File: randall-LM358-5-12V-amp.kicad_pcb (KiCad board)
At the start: 2 copper layers, 20 parts, among them J1 IN1, J2 IN2, J3 Barrel_Jack, M1 Fan_3pin, M2 Fan_3pin, Q1 TIP120, Q2 TIP120, U3 LM358

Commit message: Footprint PCB Time
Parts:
- removed the J1 at (58.9, 5.88)
- removed J2: IN2, Connector_PinHeader_2.54mm:PinHeader_1x02_P2.54mm_Vertical
- added C1: 100uF, Capacitor_THT:CP_Radial_D5.0mm_P2.00mm, F.Cu at (92.6, 23.1)
- added C2: 0.01uF, Capacitor_THT:C_Disc_D7.5mm_W5.0mm_P5.00mm, F.Cu at (83.2, 23.1)
- added C3: 100uF, Capacitor_THT:CP_Radial_D5.0mm_P2.00mm, F.Cu at (99.2, 23.1)
- added C4: 100uF, Capacitor_THT:CP_Radial_D5.0mm_P2.00mm, F.Cu at (111.8, 19.1)
- added C5: 100uF, Capacitor_THT:CP_Radial_D5.0mm_P2.00mm, F.Cu at (118.4, 19.1)
- added D1: D_Schottky, Diode_THT:D_A-405_P7.62mm_Horizontal, F.Cu at (71.9, 22.0)
- added L1: 68uH, Inductor_THT:L_Axial_L14.0mm_D4.5mm_P5.08mm_Vertical_Fastron_LACC, F.Cu at (112.4, 12.8)
- added U1: LM2674M-3.3, Package_DIP:DIP-8_W7.62mm_Socket, F.Cu at (111.5, 0.02)
- added U3: Z-Uno, ZUno:Z-UNO, F.Cu at (89.8, 8.86)
- J1: renamed from J3; footprint Connector_BarrelJack:BarrelJack_CUI_PJ-063AH_Horizontal_CircularHoles -> TerminalBlock:TerminalBlock_Altech_AK300-2_P5.00mm
- moved Q1 118.2 mm to (128.3, 64.8)
- moved Q2 99.5 mm to (127.0, 49.5)
- moved U2 97.6 mm to (99.1, 61.0)
- moved R4 81.7 mm to (99.1, 47.0)
- moved R3 69.3 mm to (66.0, 68.6)
- moved J1 16.6 mm to (15.2, 19.1)
- renumbered D1 to D2, D2 to D3, R2 to R1, R3 to R2, R4 to R3, R1 to R4, R7 to R6, R8 to R7, R9 to R8, R6 to R9, U3 to U2
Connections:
- J1 pad 1: 10-24VDC+ -> 15VDC
- J1 pad 2: 10-24VDC- -> GND

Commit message: Ok cool
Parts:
- moved R5 217.4 mm to (212.0, 132.8), turned to 90 degrees
- moved D2 213.4 mm to (213.6, 108.8), turned to 90 degrees
- moved D3 194.8 mm to (213.5, 63.7), turned to 270 degrees
- moved M1 193.9 mm to (213.6, 114.5), turned to 270 degrees
- moved R10 191.9 mm to (212.0, 94.8), turned to 90 degrees
- moved M2 177.3 mm to (213.6, 76.5), turned to 270 degrees
- moved R6 156.6 mm to (168.3, 95.9), turned to 180 degrees
- moved R9 152.1 mm to (156.2, 105.4), turned to 180 degrees
- moved R2 148.5 mm to (155.6, 88.3), turned to 180 degrees
- moved R8 148.0 mm to (168.3, 81.3), turned to 180 degrees
- moved R1 142.2 mm to (148.0, 95.9)
- moved R7 139.1 mm to (160.7, 88.3)
- moved C4 109.0 mm to (162.6, 115.6), turned to 90 degrees
- moved U3 100.7 mm to (134.6, 99.1), turned to 270 degrees
- moved C5 97.0 mm to (162.6, 105.4), turned to 90 degrees
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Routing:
- added copper zone on B.Cu, net GND
- added copper zone on F.Cu, net GND
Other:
- board outline added: 137.2 x 91.4 mm
- net class High added: clearance 0.781437, trace_width 0.781437, via_dia 0.8, via_drill 0.4

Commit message: This is it, make no mistake about it
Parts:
- J1: value Barrel_Jack -> Power
- moved D2 39.3 mm to (175.3, 100.3), turned to 270 degrees
- moved D3 38.3 mm to (175.2, 63.1)
- moved FAN1 38.3 mm to (175.3, 113.9)
- moved FAN2 38.3 mm to (175.3, 75.8)
- moved Q1 38.3 mm to (163.4, 114.2)
- moved Q2 38.3 mm to (163.4, 77.0)
- moved R5 36.8 mm to (175.3, 132.2)
- moved R10 36.7 mm to (175.3, 94.0)
- moved C1 24.4 mm to (94.5, 81.9), turned to 0 degrees
- moved U2 20.5 mm to (137.2, 76.2)
- moved R7 19.2 mm to (144.6, 98.7)
- moved R3 19.2 mm to (131.9, 91.8)
- moved R8 19.2 mm to (152.2, 91.8)
- moved R2 19.2 mm to (139.5, 98.7)
- moved U3 18.5 mm to (116.1, 98.9)
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- renumbered M1 to FAN1, M2 to FAN2
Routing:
- net 15VDC: track 0.00 -> 223.0 mm
- net TACH2: track 0.00 -> 70.3 mm
- net TACH1: track 0.00 -> 66.4 mm
- net Net-(Q1-Pad1): track 0.00 -> 59.8 mm
- net Net-(C4-Pad1): track 0.00 -> 53.9 mm
- net Net-(C5-Pad1): track 0.00 -> 39.4 mm
- net Net-(Q2-Pad1): track 0.00 -> 35.5 mm
- net Net-(C2-Pad1): track 0.00 -> 35.3 mm
- net Net-(D2-Pad2): track 0.00 -> 32.7 mm
- net Net-(D3-Pad2): track 0.00 -> 32.1 mm
- net Net-(R2-Pad1): track 0.00 -> 21.0 mm
- net 3V3DC: track 0.00 -> 19.1 mm
- net Net-(R7-Pad1): track 0.00 -> 18.3 mm
- net PWM1: track 0.00 -> 17.5 mm
- net Net-(C2-Pad2): track 0.00 -> 16.1 mm
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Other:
- board size 137.2 x 91.4 mm -> 100.3 x 77.5 mm
- net class Default: clearance 0.2 -> 0.25; trace_width 0.25 -> 0.127; via_dia 0.8 -> 0.6; via_drill 0.4 -> 0.3
- net class High removed
- rule trace_clearance: 0.2 -> 0.25
- rule trace_min: 0.2 -> 0.127
- rule via_min_size: 0.4 -> 0.6
- board text added: "15VDC"
- board text added: "Fan Controller Board"
- board text added: "GND"
- board text added: "Randall Shutt"
- board text added: "Version 0.0.1"

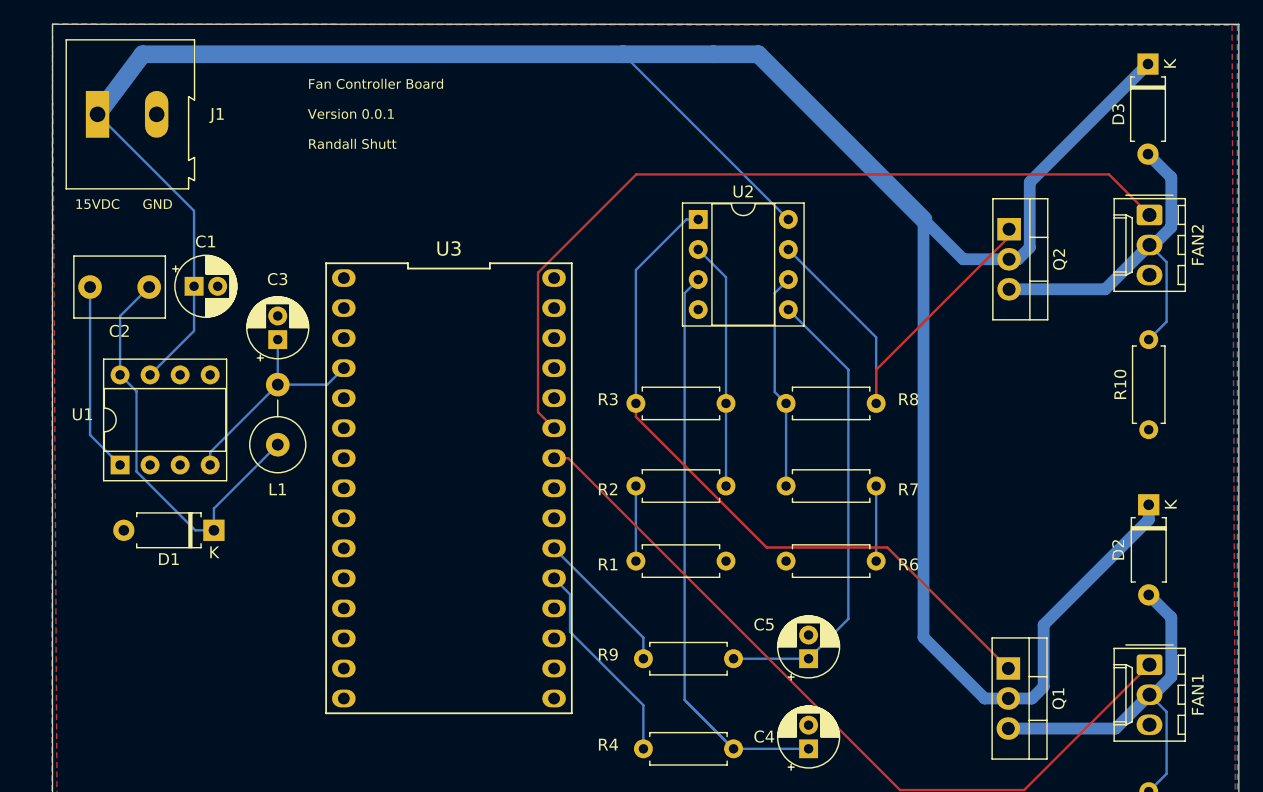
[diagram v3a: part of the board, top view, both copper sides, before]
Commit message: Added zuno module
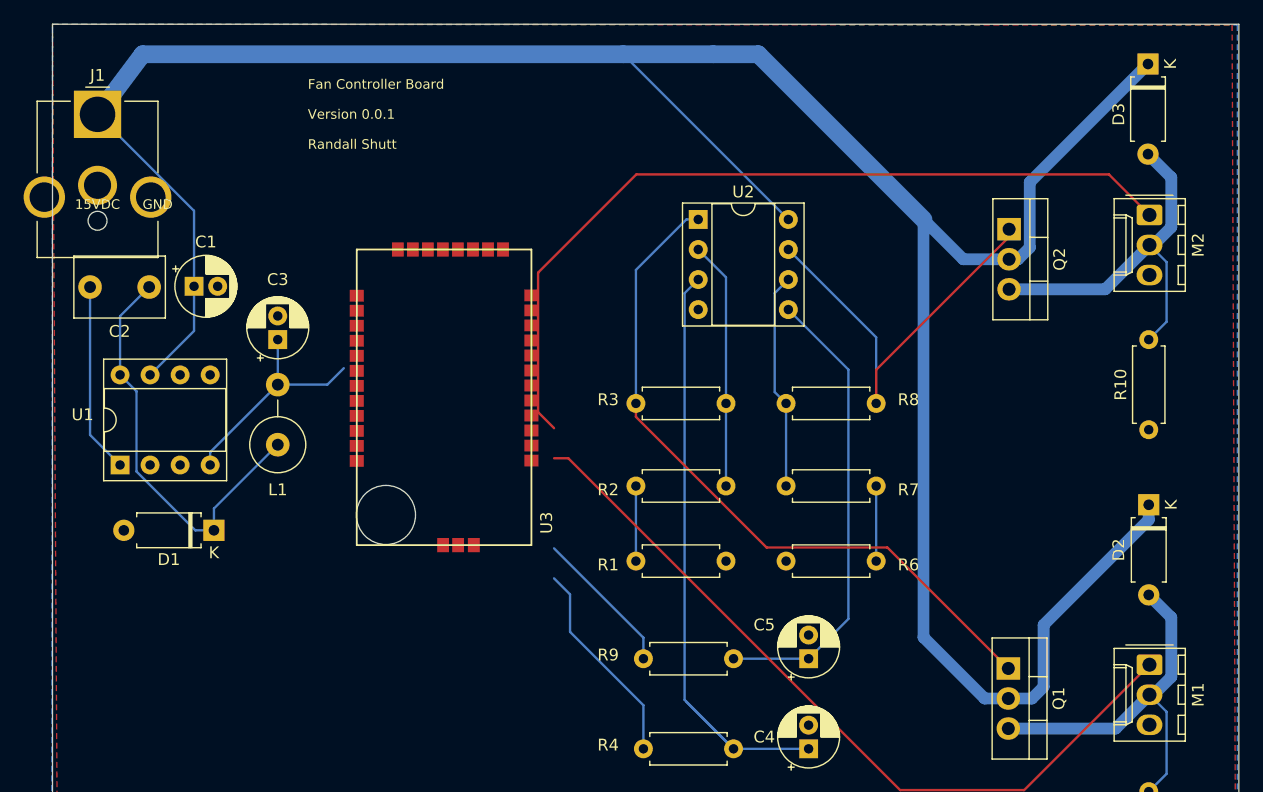
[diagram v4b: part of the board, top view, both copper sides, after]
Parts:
- J1: value Power -> Barrel_Jack; footprint TerminalBlock:TerminalBlock_Altech_AK300-2_P5.00mm -> Connector_BarrelJack:BarrelJack_CUI_PJ-063AH_Horizontal_CircularHoles
- U3: value Z-Uno -> Z-Uno-Module; footprint ZUno:Z-UNO -> ZUno Module:Z-UNO Module
- moved U3 20.6 mm to (111.8, 78.7)
- renumbered FAN1 to M1, FAN2 to M2
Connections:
- U1 pad 2: (no net) -> Net-(U1-Pad2)
- U1 pad 3: (no net) -> Net-(U1-Pad3)
- U1 pad 5: (no net) -> Net-(U1-Pad5)
- U3 pad 1: (no net) -> Net-(U3-Pad1)
- U3 pad 10: (no net) -> Net-(U3-Pad10)
- U3 pad 11: (no net) -> Net-(U3-Pad11)
- U3 pad 12: (no net) -> Net-(U3-Pad12)
- U3 pad 13: (no net) -> PWM1
- U3 pad 14: (no net) -> PWM2
- U3 pad 15: (no net) -> Net-(U3-Pad15)
- U3 pad 16: (no net) -> Net-(U3-Pad16)
- U3 pad 17: (no net) -> TACH1
- U3 pad 18: (no net) -> TACH2
- U3 pad 19: (no net) -> Net-(U3-Pad19)
- U3 pad 2: (no net) -> Net-(U3-Pad2)
- U3 pad 20: PWM1 -> Net-(U3-Pad20)
- U3 pad 21: PWM2 -> Net-(U3-Pad21)
- U3 pad 22: (no net) -> Net-(U3-Pad22)
- U3 pad 23: (no net) -> Net-(U3-Pad23)
- U3 pad 24: TACH1 -> Net-(U3-Pad24)
- U3 pad 25: TACH2 -> Net-(U3-Pad25)
- U3 pad 26: (no net) -> 3V3DC
- U3 pad 27: (no net) -> Net-(U3-Pad27)
- U3 pad 28: (no net) -> Net-(U3-Pad28)
- U3 pad 29: (no net) -> GND
- U3 pad 3: GND -> Net-(U3-Pad3)
- U3 pad 30: (no net) -> Net-(U3-Pad30)
- U3 pad 4: 3V3DC -> Net-(U3-Pad4)
- U3 pad 5: (no net) -> Net-(U3-Pad5)
- U3 pad 6: (no net) -> Net-(U3-Pad6)
- U3 pad 7: (no net) -> Net-(U3-Pad7)
- U3 pad 8: (no net) -> Net-(U3-Pad8)
- U3 pad 9: (no net) -> Net-(U3-Pad9)

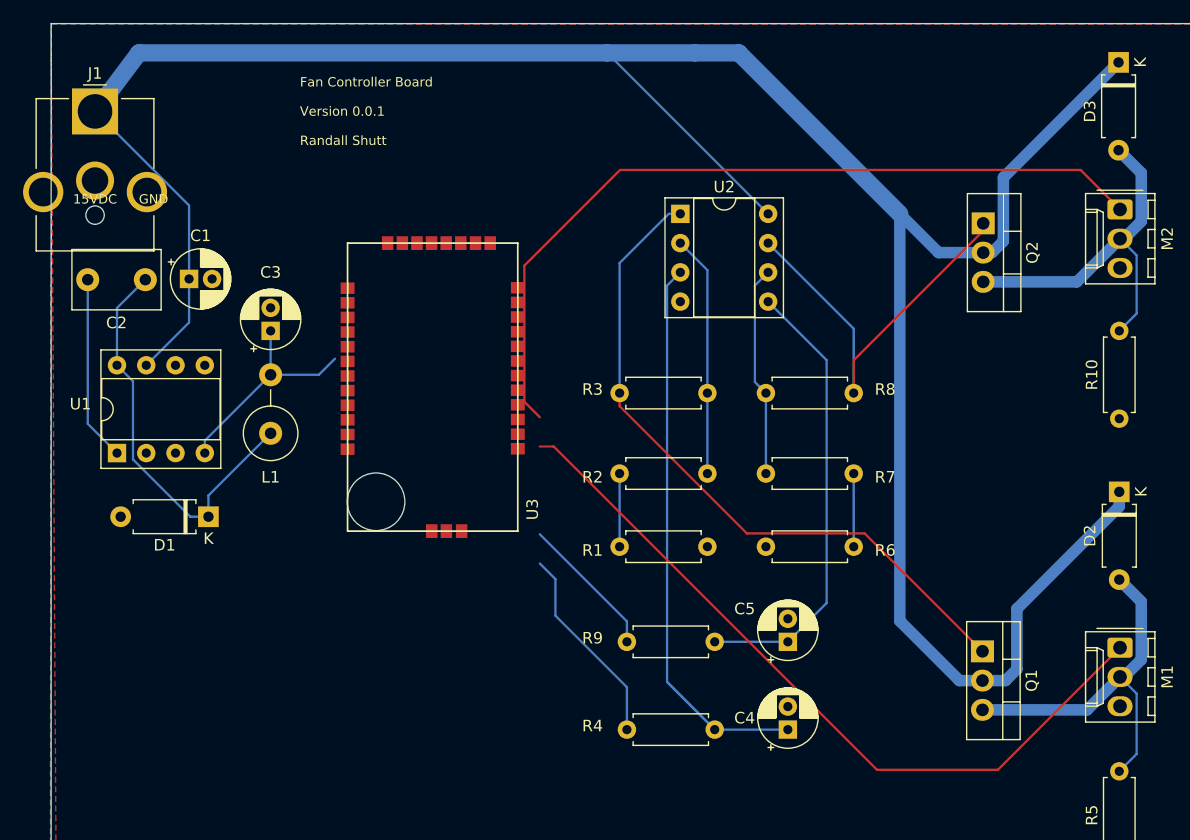
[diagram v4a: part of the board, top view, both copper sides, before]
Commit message: Ok this is probably wrong due to Via use?
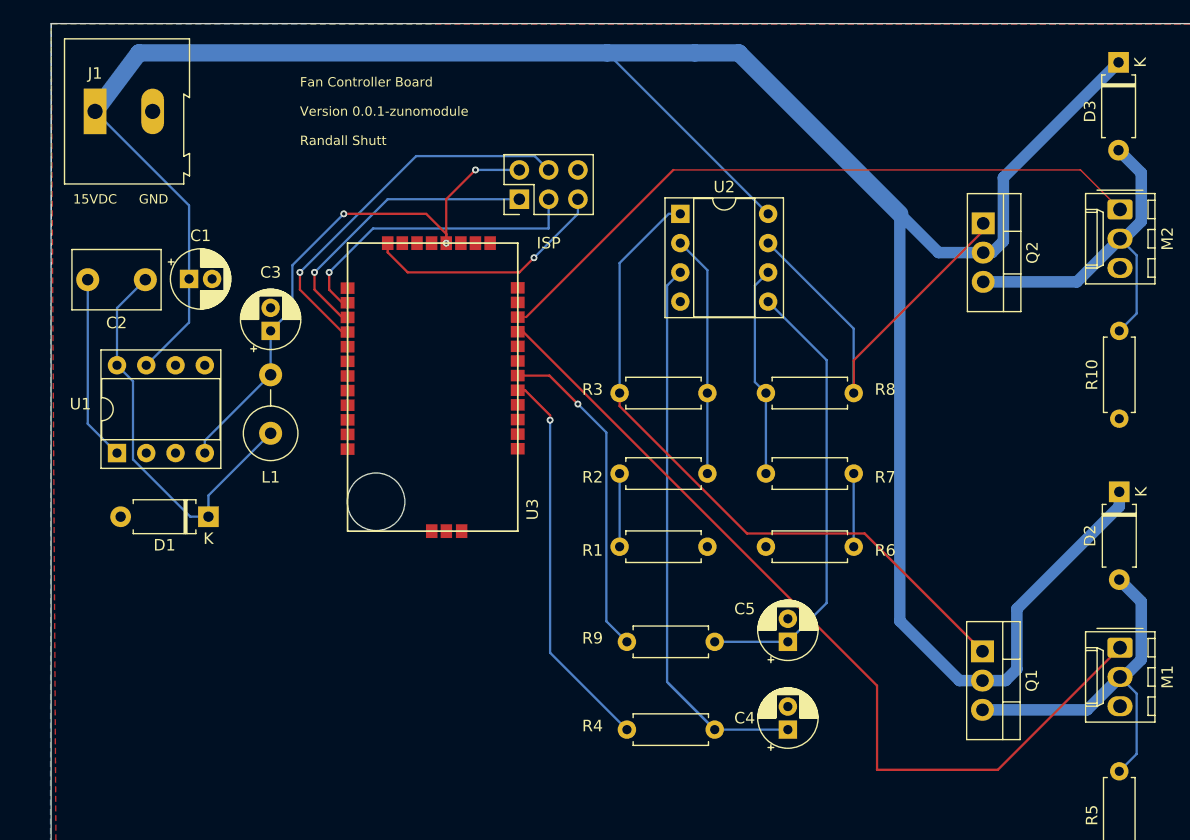
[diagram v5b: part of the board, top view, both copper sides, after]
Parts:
- added ISP: AVR-ISP-6, Connector_PinHeader_2.54mm:PinHeader_2x03_P2.54mm_Vertical, F.Cu at (123.2, 74.9)
- J1: value Barrel_Jack -> Power; footprint Connector_BarrelJack:BarrelJack_CUI_PJ-063AH_Horizontal_CircularHoles -> TerminalBlock:TerminalBlock_Altech_AK300-2_P5.00mm
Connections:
- U3 pad 0: Net-(U3-Pad0) -> SCK
- U3 pad 1: Net-(U3-Pad1) -> MISO
- U3 pad 2: Net-(U3-Pad2) -> MOSI
- U3 pad 30: Net-(U3-Pad30) -> RST
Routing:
- net MOSI: track 0.00 -> 33.4 mm, vias 0 -> 1
- net 3V3DC: track 19.1 -> 47.4 mm, vias 0 -> 3
- net SCK: track 0.00 -> 26.7 mm, vias 0 -> 1
- net MISO: track 0.00 -> 25.8 mm, vias 0 -> 1
- net RST: track 0.00 -> 21.4 mm, vias 0 -> 1
- net PWM1: track 17.5 -> 33.8 mm, vias 0 -> 1
- net PWM2: track 12.5 -> 28.6 mm, vias 0 -> 1
- net TACH2: track 70.3 -> 59.0 mm
- net TACH1: track 66.4 -> 76.7 mm
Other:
- board text added: "Version 0.0.1-zunomodule"
- board text removed: "Version 0.0.1"

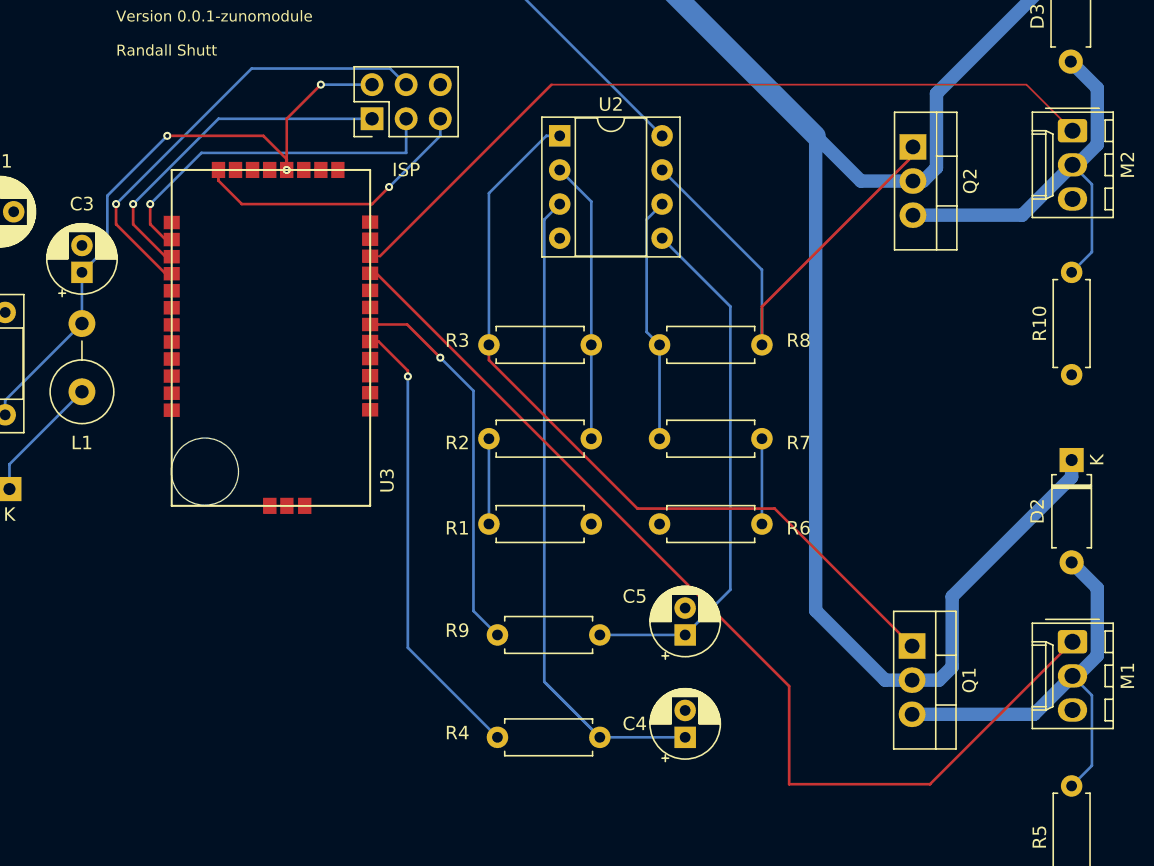
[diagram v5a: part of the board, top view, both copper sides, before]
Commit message: traces on top and aligned
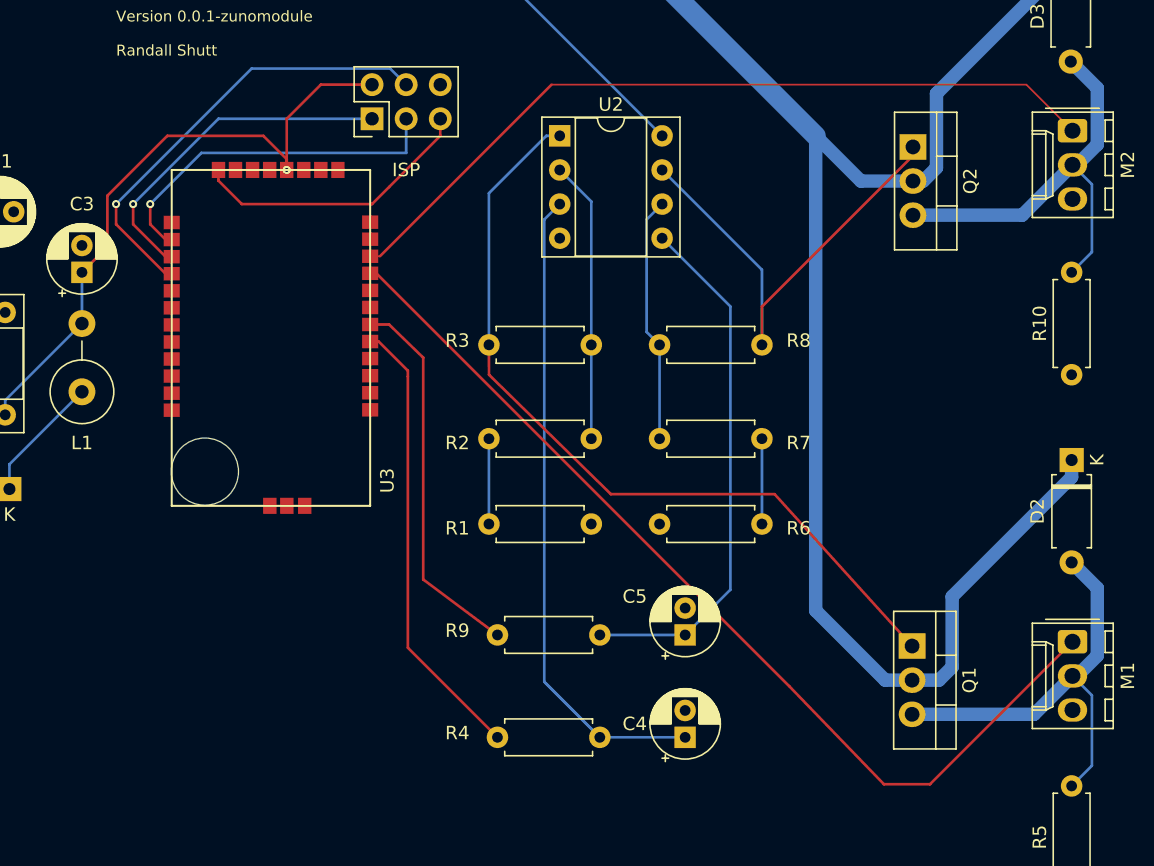
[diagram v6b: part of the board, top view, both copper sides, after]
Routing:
- net TACH1: track 76.7 -> 72.5 mm
- net Net-(Q1-Pad1): track 59.8 -> 60.7 mm
- net PWM2: track 28.6 -> 28.4 mm, vias 1 -> 0
- net RST: vias 1 -> 0
- net PWM1: vias 1 -> 0
- net 3V3DC: vias 3 -> 1
